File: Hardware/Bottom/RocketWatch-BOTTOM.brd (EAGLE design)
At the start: 160 x 100 mm, 0 parts

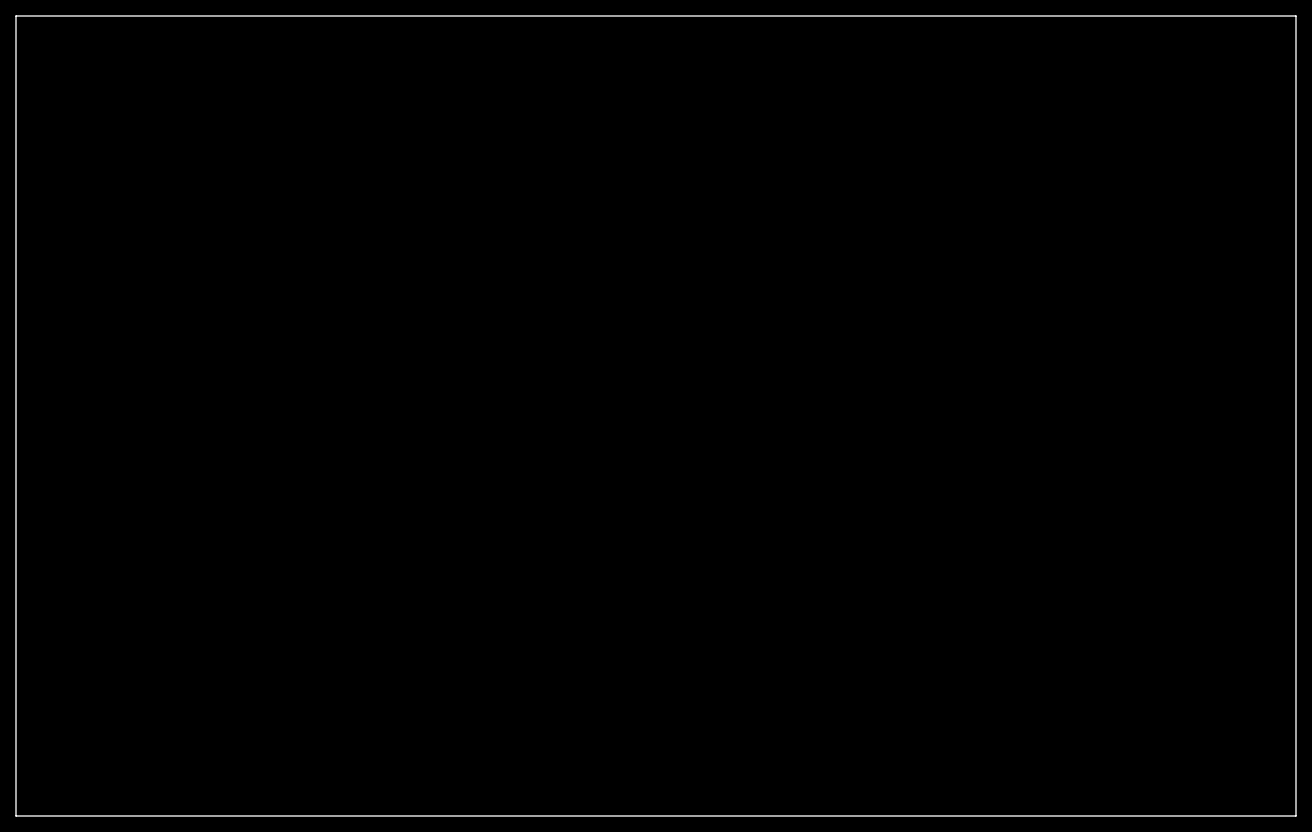
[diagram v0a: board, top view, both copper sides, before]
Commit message: finished initial layout of the bottom board and schematic
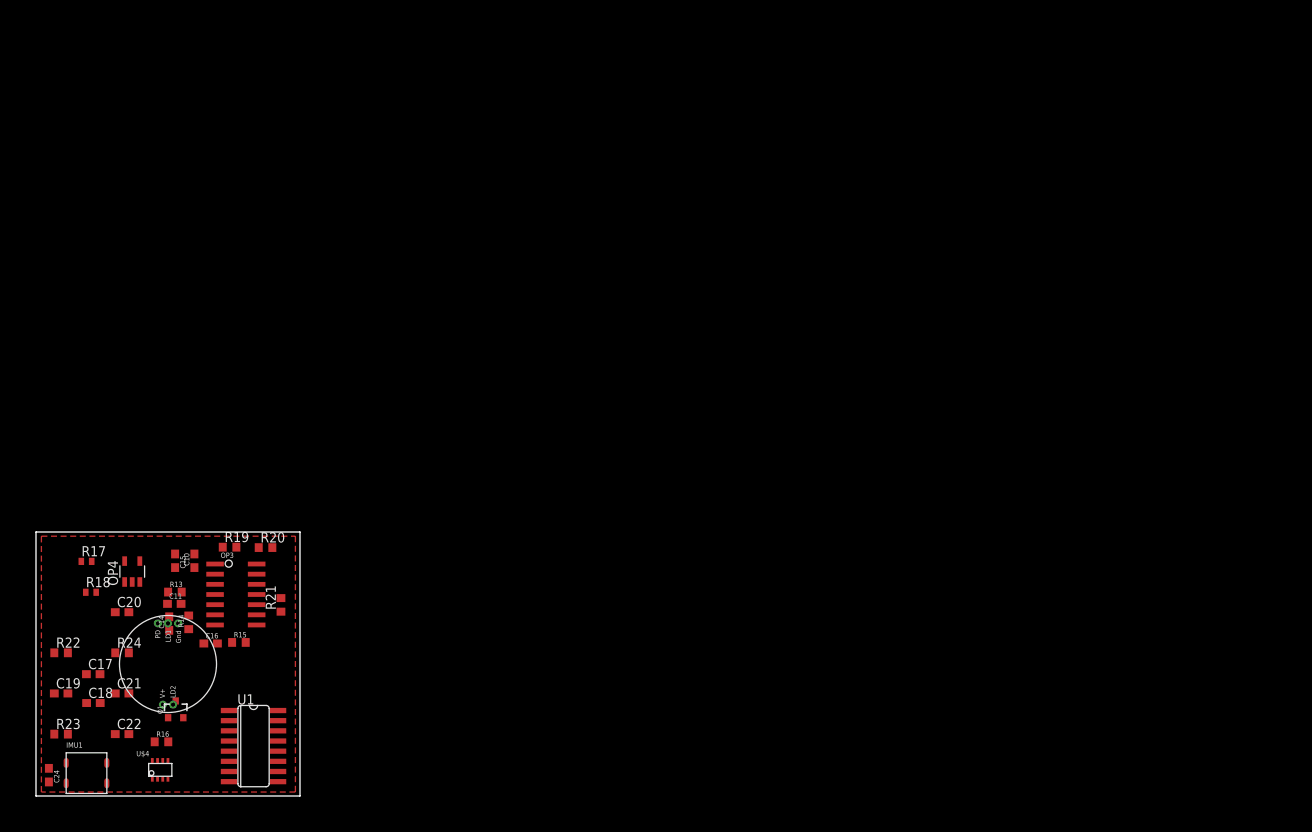
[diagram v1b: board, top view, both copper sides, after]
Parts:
- added C10, C11, C17, C18, C22, C24: 100n, LinnesLab-Passives:C0603
- added C14, C19: 2.2n, LinnesLab-Passives:C0603
- added C15, C16: 2.2u, LinnesLab-Passives:C0603
- added C20: 22u, LinnesLab-Passives:C0603
- added C21: 22n, LinnesLab-Passives:C0603
- added IMU1: LSM6DS3_CAST, LinnesLab-Sensors:LSM6DS3_CAST
- added OP3: (no value), LinnesLab-AnalogIC:SO14
- added OP4: (no value), LinnesLab-AnalogIC:SOT23-5
- added Q1: (no value), LinnesLab-DiscreteSemi:SOT23-3
- added R13, R15, R19, R21: 220k, LinnesLab-Passives:R0603
- added R14, R22: 10M, LinnesLab-Passives:R0603
- added R16: (no value), LinnesLab-Passives:R0603
- added R17, R18: 10k, LinnesLab-Passives:R0402
- added R20, R23: 1M, LinnesLab-Passives:R0603
- added R24: 10k, LinnesLab-Passives:R0603
- added U$3: (no value), LinnesLab-Connectors:PPG.MODULE.2
- added U$4: AD5171, LinnesLab-DigitalIC:SOT-23-8
- added U1: AD5242-SO16, LinnesLab-DigitalIC:SO16
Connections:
- new net 3.3V: C11.2, C17.2, C18.2, C22.2, C24.2, IMU1.2, OP3.4, OP4.5, R13.2, R15.2, R17.2, U$3.V+, U$4.2, U$4.6, U1.5, U1.6
- new net G.A1: U1.2
- new net G.A2: U1.16
- new net G.O1: U1.1
- new net G.O2: U1.13
- new net G.W2: C21.1, OP3.2, R24.1, U1.15
- new net GND: C11.1, C17.1, C18.1, C22.1, C24.1, IMU1.1, OP3.11, OP4.2, OP4.3, Q1.2, R18.1, R19.1, R21.1, U$3.GND, U$4.3, U1.10, U1.11, U1.12, U1.9
- new net LED: Q1.3
- new net LED.C: U$3.LD1
- new net LED.CTRL: U$4.8
- new net N$10: OP3.12, R17.1, R18.2
- new net N$13: C15.2, OP3.5, R13.1, R19.2
- new net N$15: C14.2, OP3.6, R14.1, R20.2
- new net N$16: C14.1, C16.1, OP3.7, R14.2
- new net N$17: C16.2, OP3.10, R15.1, R21.2
- new net N$18: C19.2, OP3.9, R22.1, R23.2
- new net N$19: C19.1, C20.1, OP3.8, R22.2
- new net N$20: C20.2, R24.2
- new net N$8: Q1.1, R16.2
- new net N$9: R16.1, U$4.1, U$4.7
- new net PD.C: C10.1, OP4.4, U$3.PD, U1.4
- new net PPG: C21.2, OP3.1, U1.14
- new net SCL: IMU1.3, U$4.4, U1.7
- new net SDA: IMU1.4, U$4.5, U1.8
- new net TIA: C10.2, C15.1, OP4.1, U1.3
- new net VREF: OP3.13, OP3.14, OP3.3, R20.1, R23.1
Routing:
- added copper zone on layer 1, net 3.3V
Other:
- board size 160 x 100 mm -> 33 x 33 mm
